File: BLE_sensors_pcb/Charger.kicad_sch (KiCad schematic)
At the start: 13 parts, among them U5 MCP73871

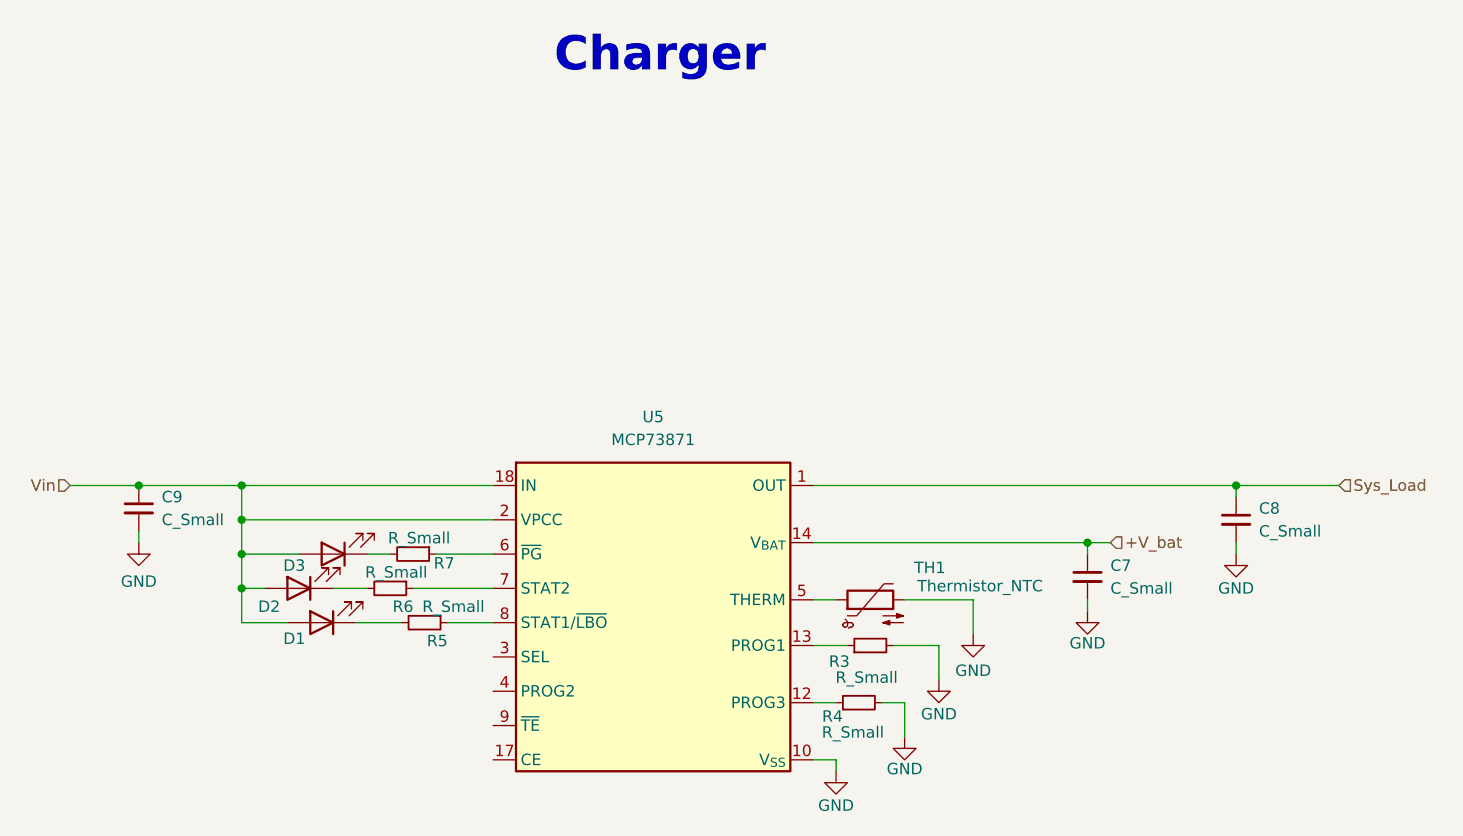
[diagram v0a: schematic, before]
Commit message: Added the usb to serial bridge
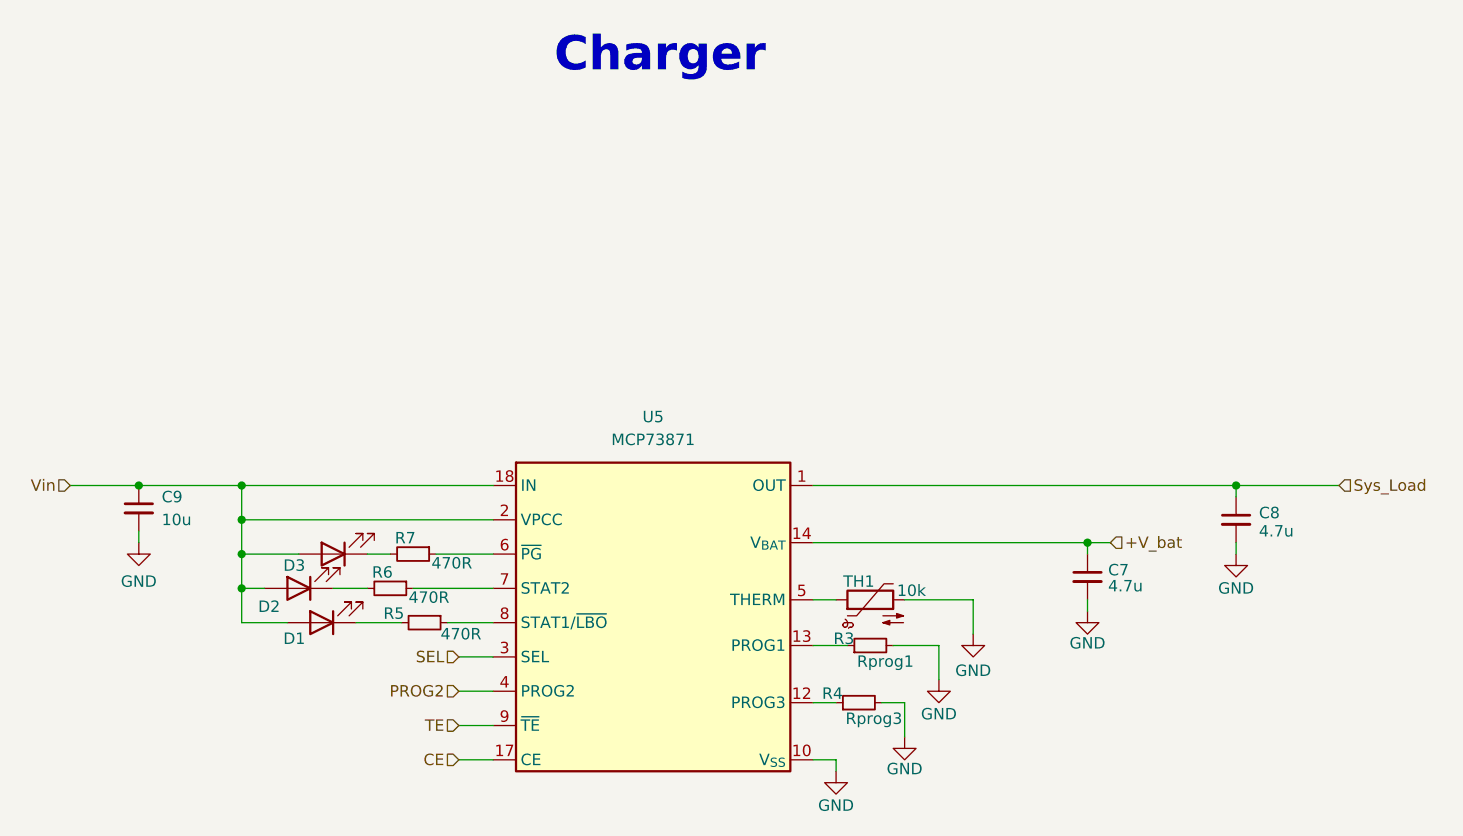
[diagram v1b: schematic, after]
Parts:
- C7, C8: value C_Small -> 4.7u
- C9: value C_Small -> 10u
- R3: value R_Small -> Rprog1
- R4: value R_Small -> Rprog3
- R5, R6, R7: value R_Small -> 470R
- TH1: value Thermistor_NTC -> 10k
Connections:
- net CE: now reaches U5.17 (CE)
- net SEL: now reaches U5.3 (SEL)
- net PROG2: now reaches U5.4 (PROG2)
- net TE: now reaches U5.9 (~{TE})
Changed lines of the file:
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@@
+	(wire
+		(pts
+			(xy 121.92 113.03) (xy 125.73 113.03)
+		)
+		(stroke
+			(width 0)
+			(type default)
+		)
+	)
 	(wire
 		(pts
@@
 	(wire
 		(pts
+			(xy 121.92 101.6) (xy 125.73 101.6)
+		)
+		(stroke
+			(width 0)
+			(type default)
+		)
+	)
+	(wire
+		(pts
 			(xy 97.79 93.98) (xy 100.33 93.98)
 		)
@@
 	(wire
 		(pts
+			(xy 121.92 109.22) (xy 125.73 109.22)
+		)
+		(stroke
+			(width 0)
+			(type default)
+		)
+	)
+	(wire
+		(pts
 			(xy 97.79 82.55) (xy 125.73 82.55)
 		)
@@
 		(pts
 			(xy 161.29 95.25) (xy 163.83 95.25)
+		)
+		(stroke
+			(width 0)
+			(type default)
+		)
+	)
+	(wire
+		(pts
+			(xy 121.92 105.41) (xy 125.73 105.41)
 		)
 		(stroke
@@
 		)
 	)
+	(hierarchical_label "TE"
+		(shape input)
+		(at 121.92 109.22 180)
+		(effects
+			(font
+				(size 1.27 1.27)
+			)
+			(justify right)
+		)
+	)
+	(hierarchical_label "CE"
+		(shape input)
+		(at 121.92 113.03 180)
+		(effects
+			(font
+				(size 1.27 1.27)
+			)
+			(justify right)
+		)
+	)
 	(hierarchical_label "+V_bat"
 		(shape input)
@@
 		)
 	)
+	(hierarchical_label "SEL"
+		(shape input)
+		(at 121.92 101.6 180)
+		(effects
+			(font
+				(size 1.27 1.27)
+			)
+			(justify right)
+		)
+	)
+	(hierarchical_label "PROG2"
+		(shape input)
+		(at 121.92 105.41 180)
+		(effects
+			(font
+				(size 1.27 1.27)
+			)
+			(justify right)
+		)
+	)
 	(hierarchical_label "Vin"
 		(shape input)
@@
 		(dnp no)
 		(property "Reference" "TH1"
-			(at 174.244 91.694 90)
-			(effects
-				(font
-					(size 1.27 1.27)
-				)
-			)
-		)
-		(property "Value" "Thermistor_NTC"
-			(at 179.832 93.726 90)
+			(at 166.37 93.218 90)
+			(effects
+				(font
+					(size 1.27 1.27)
+				)
+			)
+		)
+		(property "Value" "10k"
+			(at 172.212 94.234 90)
 			(effects
 				(font
@@
 		(dnp no)
 		(property "Reference" "R6"
-			(at 114.554 96.012 90)
+			(at 112.268 92.202 90)
 			(effects
 				(font
@@
 			)
 		)
-		(property "Value" "R_Small"
-			(at 111.506 92.202 90)
+		(property "Value" "470R"
+			(at 116.332 94.996 90)
 			(effects
 				(font
@@
 		(dnp no)
 		(property "Reference" "R3"
-			(at 165.354 102.108 90)
+			(at 165.862 99.568 90)
 			(effects
 				(font
@@
 			)
 		)
-		(property "Value" "R_Small"
-			(at 170.688 103.886 90)
+		(property "Value" "Rprog1"
+			(at 172.466 102.108 90)
 			(effects
 				(font
@@
 		(dnp no)
 		(property "Reference" "R7"
-			(at 119.126 91.186 90)
+			(at 114.808 88.392 90)
 			(effects
 				(font
@@
 			)
 		)
-		(property "Value" "R_Small"
-			(at 114.046 88.392 90)
+		(property "Value" "470R"
+			(at 118.872 91.186 90)
 			(effects
 				(font
@@
 		(dnp no)
 		(property "Reference" "R4"
-			(at 164.592 108.204 90)
+			(at 164.592 105.664 90)
 			(effects
 				(font
@@
 			)
 		)
-		(property "Value" "R_Small"
-			(at 169.164 109.982 90)
+		(property "Value" "Rprog3"
+			(at 171.196 108.458 90)
 			(effects
 				(font
@@
 		(on_board yes)
 		(dnp no)
-		(fields_autoplaced yes)
 		(property "Reference" "C7"
-			(at 194.31 91.4462 0)
+			(at 194.056 91.948 0)
 			(effects
 				(font
@@
 			)
 		)
-		(property "Value" "C_Small"
-			(at 194.31 93.9862 0)
+		(property "Value" "4.7u"
+			(at 194.056 93.726 0)
 			(effects
 				(font
@@
 		(dnp no)
 		(property "Reference" "R5"
-			(at 118.364 99.822 90)
+			(at 113.538 96.774 90)
 			(effects
 				(font
@@
 			)
 		)
-		(property "Value" "R_Small"
-			(at 117.856 96.012 90)
+		(property "Value" "470R"
+			(at 119.888 99.06 90)
 			(effects
 				(font
@@
 		(on_board yes)
 		(dnp no)
-		(fields_autoplaced yes)
 		(property "Reference" "C8"
-			(at 210.82 85.0962 0)
+			(at 210.82 85.598 0)
 			(effects
 				(font
@@
 			)
 		)
-		(property "Value" "C_Small"
-			(at 210.82 87.6362 0)
+		(property "Value" "4.7u"
+			(at 210.82 87.63 0)
 			(effects
 				(font
@@
 			)
 		)
-		(property "Value" "C_Small"
+		(property "Value" "10u"
 			(at 88.9 86.3662 0)
 			(effects

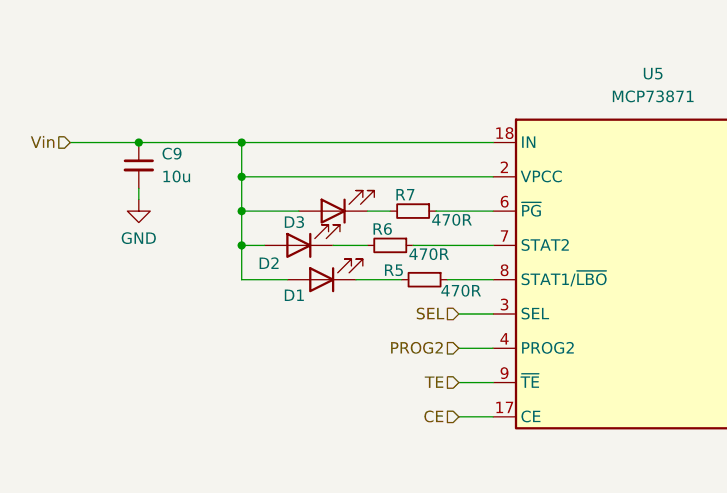
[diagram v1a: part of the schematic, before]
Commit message: Footprints and some pcb placement
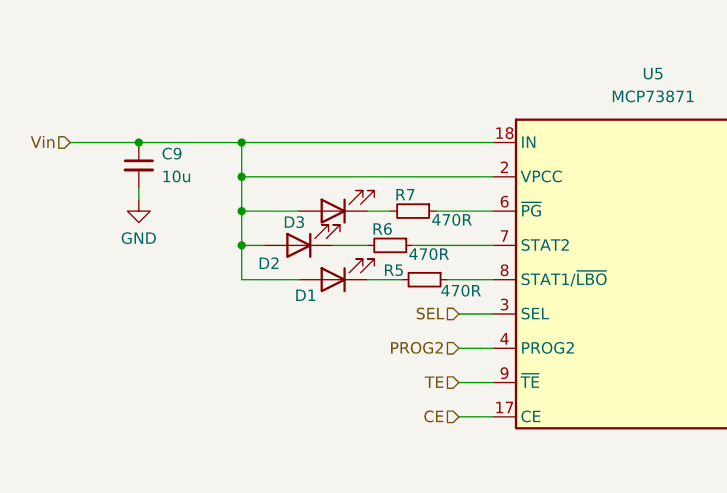
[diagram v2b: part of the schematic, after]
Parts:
- D1, D2, D3: footprint (none) -> LED_SMD:LED_0603_1608Metric
- R3, R4, R5, R6, R7, TH1: footprint (none) -> Resistor_SMD:R_0603_1608Metric
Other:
- moved on the sheet: D1
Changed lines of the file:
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@@
 	(wire
 		(pts
-			(xy 110.49 97.79) (xy 115.57 97.79)
+			(xy 111.76 97.79) (xy 115.57 97.79)
 		)
 		(stroke
@@
 	(wire
 		(pts
-			(xy 102.87 97.79) (xy 97.79 97.79)
+			(xy 104.14 97.79) (xy 97.79 97.79)
 		)
 		(stroke
@@
 			)
 		)
-		(property "Footprint" ""
+		(property "Footprint" "Resistor_SMD:R_0603_1608Metric"
 			(at 166.37 95.25 0)
 			(effects
@@
 			)
 		)
-		(property "Footprint" ""
+		(property "Footprint" "Resistor_SMD:R_0603_1608Metric"
 			(at 114.3 93.98 0)
 			(effects
@@
 			)
 		)
-		(property "Footprint" ""
+		(property "Footprint" "Resistor_SMD:R_0603_1608Metric"
 			(at 167.64 100.33 0)
 			(effects
@@
 			)
 		)
-		(property "Footprint" ""
+		(property "Footprint" "Resistor_SMD:R_0603_1608Metric"
 			(at 116.84 90.17 0)
 			(effects
@@
 			)
 		)
-		(property "Footprint" ""
+		(property "Footprint" "Resistor_SMD:R_0603_1608Metric"
 			(at 166.37 106.68 0)
 			(effects
@@
 			)
 		)
-		(property "Footprint" ""
+		(property "Footprint" "LED_SMD:LED_0603_1608Metric"
 			(at 107.95 90.17 0)
 			(effects
@@
 	(symbol
 		(lib_id "Device:LED")
-		(at 106.68 97.79 180)
+		(at 107.95 97.79 180)
 		(unit 1)
 		(exclude_from_sim no)
@@
 		(dnp no)
 		(property "Reference" "D1"
-			(at 103.632 99.568 0)
+			(at 104.902 99.568 0)
 			(effects
 				(font
@@
 		)
 		(property "Value" "LED"
-			(at 103.378 96.266 0)
-			(effects
-				(font
-					(size 1.27 1.27)
-				)
-				(hide yes)
-			)
-		)
-		(property "Footprint" ""
-			(at 106.68 97.79 0)
+			(at 104.648 96.266 0)
+			(effects
+				(font
+					(size 1.27 1.27)
+				)
+				(hide yes)
+			)
+		)
+		(property "Footprint" "LED_SMD:LED_0603_1608Metric"
+			(at 107.95 97.79 0)
 			(effects
 				(font
@@
 		)
 		(property "Datasheet" "~"
-			(at 106.68 97.79 0)
+			(at 107.95 97.79 0)
 			(effects
 				(font
@@
 		)
 		(property "Description" "Light emitting diode"
-			(at 106.68 97.79 0)
+			(at 107.95 97.79 0)
 			(effects
 				(font
@@
 		)
 		(property "Sim.Pins" "1=K 2=A"
-			(at 106.68 97.79 0)
+			(at 107.95 97.79 0)
 			(effects
 				(font
@@
 			)
 		)
-		(property "Footprint" ""
+		(property "Footprint" "Resistor_SMD:R_0603_1608Metric"
 			(at 118.11 97.79 0)
 			(effects
@@
 			)
 		)
-		(property "Footprint" ""
+		(property "Footprint" "LED_SMD:LED_0603_1608Metric"
 			(at 104.14 93.98 0)
 			(effects

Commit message: Initial pcb placement
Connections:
- net CE is gone; now on net Vin: U5.17 (CE)
- net PROG2 is gone; now on net Vin: U5.4 (PROG2)
- net SEL is gone; now on net GND: U5.3 (SEL)
- net TE is gone; now on net Vin: U5.9 (~{TE})
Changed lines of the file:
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@@
+	(wire
+		(pts
+			(xy 111.76 97.79) (xy 115.57 97.79)
+		)
+		(stroke
+			(width 0)
+			(type default)
+		)
+	)
+	(wire
+		(pts
+			(xy 116.84 93.98) (xy 125.73 93.98)
+		)
+		(stroke
+			(width 0)
+			(type default)
+		)
+	)
+	(wire
+		(pts
+			(xy 175.26 100.33) (xy 175.26 104.14)
+		)
+		(stroke
+			(width 0)
+			(type default)
+		)
+	)
+	(wire
+		(pts
+			(xy 97.79 86.36) (xy 97.79 90.17)
+		)
+		(stroke
+			(width 0)
+			(type default)
+		)
+	)
+	(wire
+		(pts
+			(xy 114.3 101.6) (xy 125.73 101.6)
+		)
+		(stroke
+			(width 0)
+			(type default)
+		)
+	)
+	(wire
+		(pts
+			(xy 208.28 83.82) (xy 208.28 82.55)
+		)
+		(stroke
+			(width 0)
+			(type default)
+		)
+	)
+	(wire
+		(pts
+			(xy 191.77 88.9) (xy 191.77 90.17)
+		)
+		(stroke
+			(width 0)
+			(type default)
+		)
+	)
+	(wire
+		(pts
+			(xy 161.29 100.33) (xy 165.1 100.33)
+		)
+		(stroke
+			(width 0)
+			(type default)
+		)
+	)
+	(wire
+		(pts
+			(xy 78.74 82.55) (xy 86.36 82.55)
+		)
+		(stroke
+			(width 0)
+			(type default)
+		)
+	)
+	(wire
+		(pts
+			(xy 86.36 82.55) (xy 97.79 82.55)
+		)
+		(stroke
+			(width 0)
+			(type default)
+		)
+	)
+	(wire
+		(pts
+			(xy 161.29 88.9) (xy 191.77 88.9)
+		)
+		(stroke
+			(width 0)
+			(type default)
+		)
+	)
+	(wire
+		(pts
+			(xy 114.3 104.14) (xy 114.3 101.6)
+		)
+		(stroke
+			(width 0)
+			(type default)
+		)
+	)
+	(wire
+		(pts
+			(xy 179.07 95.25) (xy 179.07 99.06)
+		)
+		(stroke
+			(width 0)
+			(type default)
+		)
+	)
+	(wire
+		(pts
+			(xy 97.79 93.98) (xy 100.33 93.98)
+		)
+		(stroke
+			(width 0)
+			(type default)
+		)
+	)
+	(wire
+		(pts
+			(xy 97.79 82.55) (xy 97.79 86.36)
+		)
+		(stroke
+			(width 0)
+			(type default)
+		)
+	)
+	(wire
+		(pts
+			(xy 161.29 82.55) (xy 208.28 82.55)
+		)
+		(stroke
+			(width 0)
+			(type default)
+		)
+	)
 	(wire
 		(pts
@@
 	(wire
 		(pts
-			(xy 111.76 97.79) (xy 115.57 97.79)
-		)
-		(stroke
-			(width 0)
-			(type default)
-		)
-	)
-	(wire
-		(pts
-			(xy 116.84 93.98) (xy 125.73 93.98)
-		)
-		(stroke
-			(width 0)
-			(type default)
-		)
-	)
-	(wire
-		(pts
-			(xy 175.26 100.33) (xy 175.26 104.14)
-		)
-		(stroke
-			(width 0)
-			(type default)
-		)
-	)
-	(wire
-		(pts
-			(xy 97.79 86.36) (xy 97.79 90.17)
-		)
-		(stroke
-			(width 0)
-			(type default)
-		)
-	)
-	(wire
-		(pts
-			(xy 208.28 83.82) (xy 208.28 82.55)
-		)
-		(stroke
-			(width 0)
-			(type default)
-		)
-	)
-	(wire
-		(pts
-			(xy 191.77 88.9) (xy 191.77 90.17)
-		)
-		(stroke
-			(width 0)
-			(type default)
-		)
-	)
-	(wire
-		(pts
-			(xy 161.29 100.33) (xy 165.1 100.33)
-		)
-		(stroke
-			(width 0)
-			(type default)
-		)
-	)
-	(wire
-		(pts
-			(xy 78.74 82.55) (xy 86.36 82.55)
-		)
-		(stroke
-			(width 0)
-			(type default)
-		)
-	)
-	(wire
-		(pts
-			(xy 86.36 82.55) (xy 97.79 82.55)
-		)
-		(stroke
-			(width 0)
-			(type default)
-		)
-	)
-	(wire
-		(pts
-			(xy 161.29 88.9) (xy 191.77 88.9)
-		)
-		(stroke
-			(width 0)
-			(type default)
-		)
-	)
-	(wire
-		(pts
-			(xy 179.07 95.25) (xy 179.07 99.06)
-		)
-		(stroke
-			(width 0)
-			(type default)
-		)
-	)
-	(wire
-		(pts
-			(xy 121.92 101.6) (xy 125.73 101.6)
-		)
-		(stroke
-			(width 0)
-			(type default)
-		)
-	)
-	(wire
-		(pts
-			(xy 97.79 93.98) (xy 100.33 93.98)
-		)
-		(stroke
-			(width 0)
-			(type default)
-		)
-	)
-	(wire
-		(pts
-			(xy 97.79 82.55) (xy 97.79 86.36)
-		)
-		(stroke
-			(width 0)
-			(type default)
-		)
-	)
-	(wire
-		(pts
-			(xy 161.29 82.55) (xy 208.28 82.55)
-		)
-		(stroke
-			(width 0)
-			(type default)
-		)
-	)
-	(wire
-		(pts
 			(xy 170.18 100.33) (xy 175.26 100.33)
 		)
@@
 	(wire
 		(pts
+			(xy 121.92 105.41) (xy 125.73 105.41)
+		)
+		(stroke
+			(width 0)
+			(type default)
+		)
+	)
+	(wire
+		(pts
 			(xy 86.36 88.9) (xy 86.36 87.63)
 		)
@@
 		(pts
 			(xy 161.29 95.25) (xy 163.83 95.25)
-		)
-		(stroke
-			(width 0)
-			(type default)
-		)
-	)
-	(wire
-		(pts
-			(xy 121.92 105.41) (xy 125.73 105.41)
 		)
 		(stroke
@@
 		)
 	)
-	(hierarchical_label "TE"
-		(shape input)
-		(at 121.92 109.22 180)
-		(effects
-			(font
-				(size 1.27 1.27)
-			)
-			(justify right)
-		)
-	)
-	(hierarchical_label "CE"
-		(shape input)
-		(at 121.92 113.03 180)
-		(effects
-			(font
-				(size 1.27 1.27)
-			)
-			(justify right)
-		)
-	)
 	(hierarchical_label "+V_bat"
 		(shape input)
@@
 		)
 	)
-	(hierarchical_label "SEL"
-		(shape input)
-		(at 121.92 101.6 180)
-		(effects
-			(font
-				(size 1.27 1.27)
-			)
-			(justify right)
-		)
-	)
-	(hierarchical_label "PROG2"
+	(hierarchical_label "Vin"
 		(shape input)
 		(at 121.92 105.41 180)
@@
 	(hierarchical_label "Vin"
 		(shape input)
+		(at 121.92 113.03 180)
+		(effects
+			(font
+				(size 1.27 1.27)
+			)
+			(justify right)
+		)
+	)
+	(hierarchical_label "Vin"
+		(shape input)
 		(at 78.74 82.55 180)
+		(effects
+			(font
+				(size 1.27 1.27)
+			)
+			(justify right)
+		)
+	)
+	(hierarchical_label "Vin"
+		(shape input)
+		(at 121.92 109.22 180)
 		(effects
 			(font
@@
 					(unit 1)
 				)
+			)
+		)
+	)
+	(symbol
+		(lib_id "power:GND")
+		(at 114.3 104.14 0)
+		(unit 1)
+		(exclude_from_sim no)
+		(in_bom yes)
+		(on_board yes)
+		(dnp no)
+		(property "Reference" "#PWR049"
+			(at 114.3 110.49 0)
+			(effects
+				(font
+					(size 1.27 1.27)
+				)
+				(hide yes)
+			)
+		)
+		(property "Value" "GND"
+			(at 114.3 107.95 0)
+			(effects
+				(font
+					(size 1.27 1.27)
+				)
+			)
+		)
+		(property "Footprint" ""
+			(at 114.3 104.14 0)
+			(effects
+				(font
+					(size 1.27 1.27)
+				)
+				(hide yes)
+			)
+		)
+		(property "Datasheet" ""
+			(at 114.3 104.14 0)
+			(effects
+				(font
+					(size 1.27 1.27)
+				)
+				(hide yes)
+			)
+		)
+		(property "Description" "Power symbol creates a global label with name \"GND\" , ground"
+			(at 114.3 104.14 0)
+			(effects
+				(font
+					(size 1.27 1.27)
+				)
+				(hide yes)
+			)
+		)
+		(pin "1"
+		)
+		(instances
+			(project "BLE_sensors"
+				(path "/06b47d3c-6b7b-411b-8755-cae193722202/30528618-a979-4bf1-b774-eef2b8cf727d/9515a31a-8844-493e-b588-3303487459e9"
+					(reference "#PWR049")
+					(unit 1)
+				)
